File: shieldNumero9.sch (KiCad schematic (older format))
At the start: 0 parts

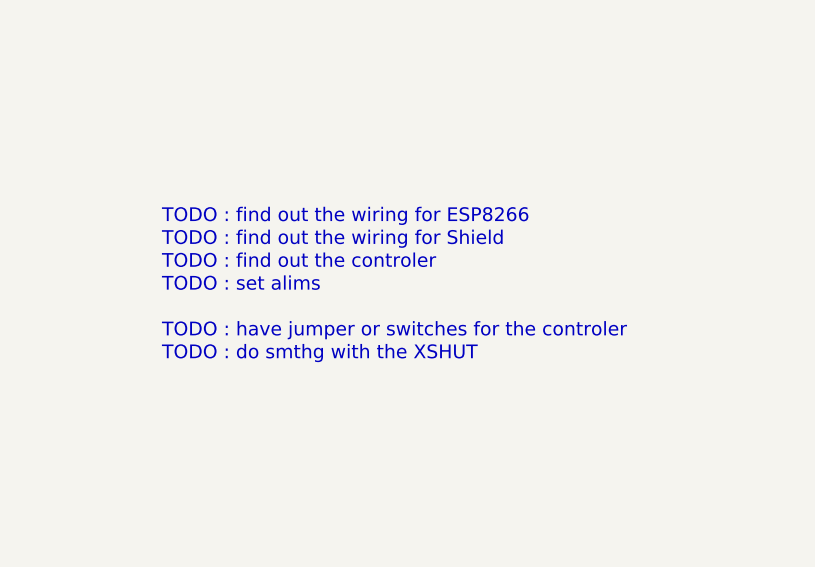
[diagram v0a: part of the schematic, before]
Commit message: finish schematics. add componants, find right chip, firest verification OK, ready for routing
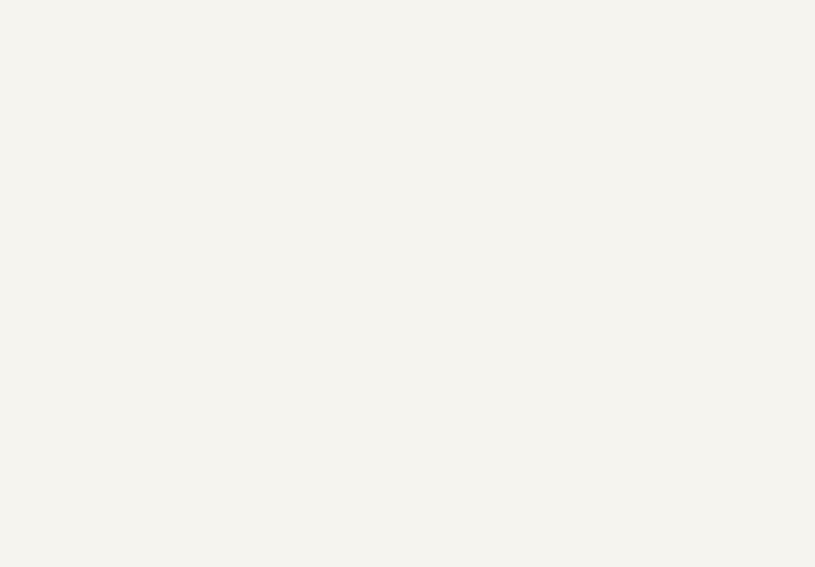
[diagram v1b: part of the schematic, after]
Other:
- note removed: "TODO : do smthg with the XSHUT"
- note removed: "TODO : find out the controler"
- note removed: "TODO : find out the wiring for ESP8266\n"
- note removed: "TODO : find out the wiring for Shield\n"
- note removed: "TODO : have jumper or switches for the controler"
- note removed: "TODO : set alims"
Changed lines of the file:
@@
 Comment4 ""
 $EndDescr
-Text Notes 4150 2600 0    60   ~ 0
-TODO : find out the wiring for Shield\n
-Text Notes 4150 2500 0    60   ~ 0
-TODO : find out the wiring for ESP8266\n
-Text Notes 4150 2800 0    60   ~ 0
-TODO : set alims
-Text Notes 4150 2700 0    60   ~ 0
-TODO : find out the controler
-Text Notes 4150 3000 0    60   ~ 0
-TODO : have jumper or switches for the controler
-Text Notes 4150 3100 0    60   ~ 0
-TODO : do smthg with the XSHUT
 $Sheet
 S 1050 900  1250 500
